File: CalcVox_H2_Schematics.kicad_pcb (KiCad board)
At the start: 4 copper layers, 118.1 x 170.2 mm, 69 parts, among them J1 Battery_Barrel_Jack, J2 AudioJack3_SwitchTR, SW1-25 SW_Push, SW1-26 SW_Push, SW1-27 SW_Push, SW1-28 SW_Push, SW1-29 SW_Push, SW1-30 SW_Push, SW1-31 SW_Push, SW1-32 SW_Push, SW2-25 SW_Push, SW2-26 SW_Push, SW2-27 SW_Push, SW2-28 SW_Push, SW2-29 SW_Push, SW2-30 SW_Push, SW2-31 SW_Push, SW2-32 SW_Push, SW3-25 SW_Push, SW3-26 SW_Push, SW3-27 SW_Push, SW3-28 SW_Push, SW3-29 SW_Push, SW3-30 SW_Push, SW3-31 SW_Push, SW3-32 SW_Push, SW4-25 SW_Push, SW4-26 SW_Push, SW4-27 SW_Push, SW4-28 SW_Push, SW4-29 SW_Push, SW4-30 SW_Push, SW4-31 SW_Push, SW4-32 SW_Push, SW5-25 SW_Push, SW5-26 SW_Push, SW5-27 SW_Push, SW5-28 SW_Push, SW5-29 SW_Push, SW5-30 SW_Push, SW5-31 SW_Push, SW5-32 SW_Push, SW6-25 SW_Push, SW6-26 SW_Push, SW6-27 SW_Push, SW6-28 SW_Push, SW6-29 SW_Push, SW6-30 SW_Push, SW6-31 SW_Push, SW6-32 SW_Push, U1 Teensy4.1, U2 MOUDLE-SEEEDUINO-XIAO-ESP32S3

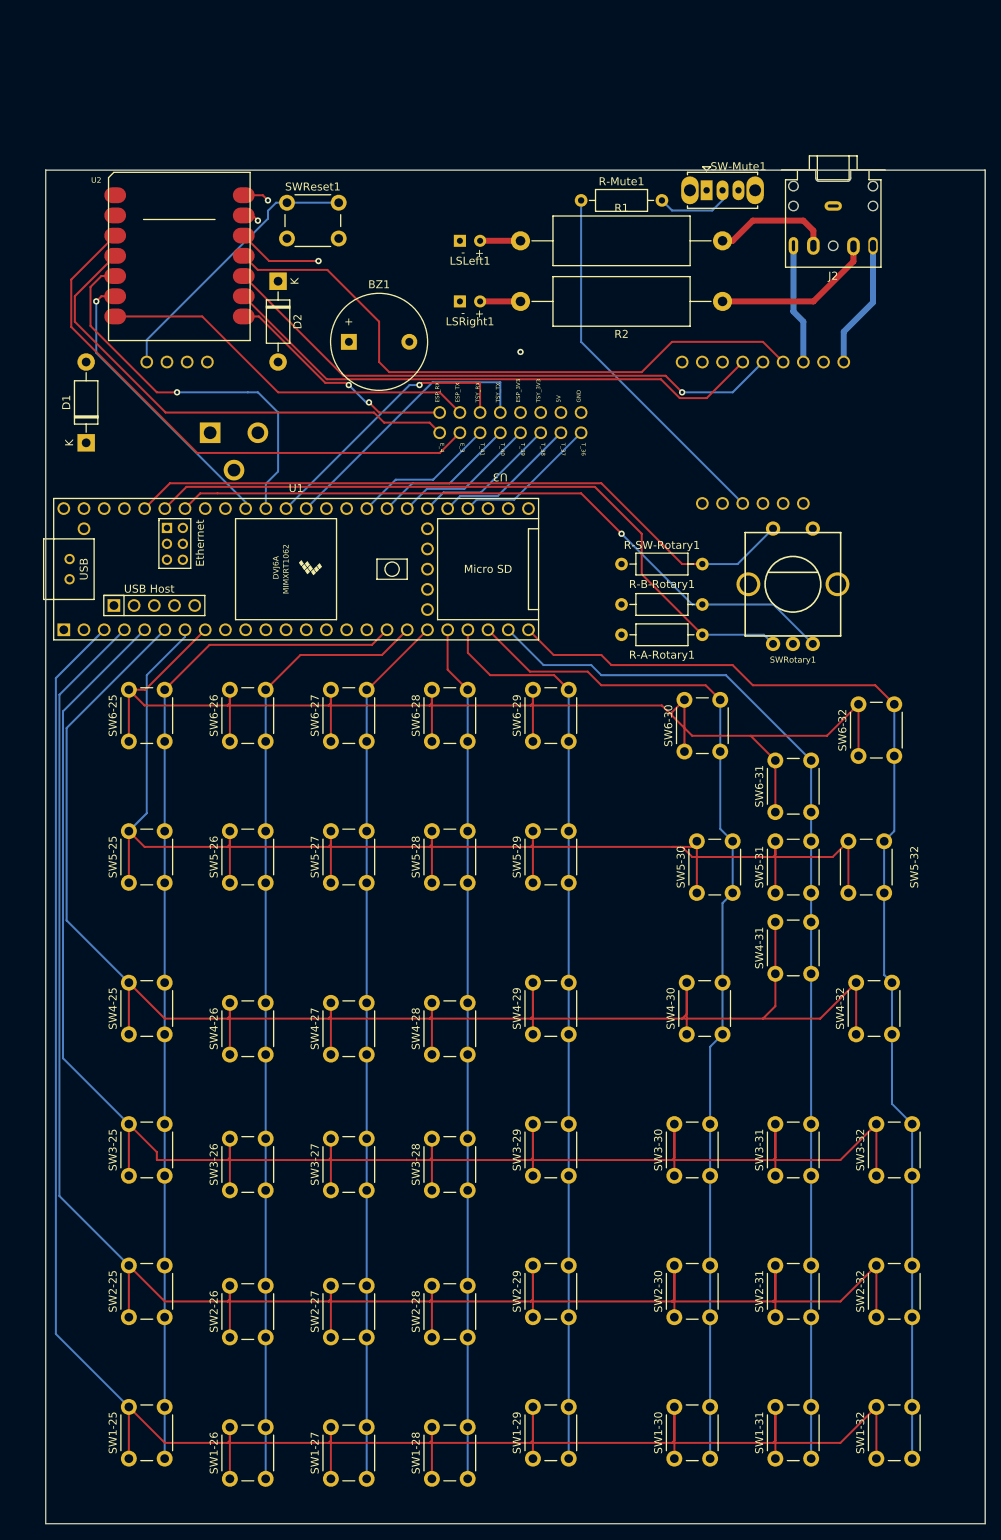
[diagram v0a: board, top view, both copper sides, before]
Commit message: Small change to move board up
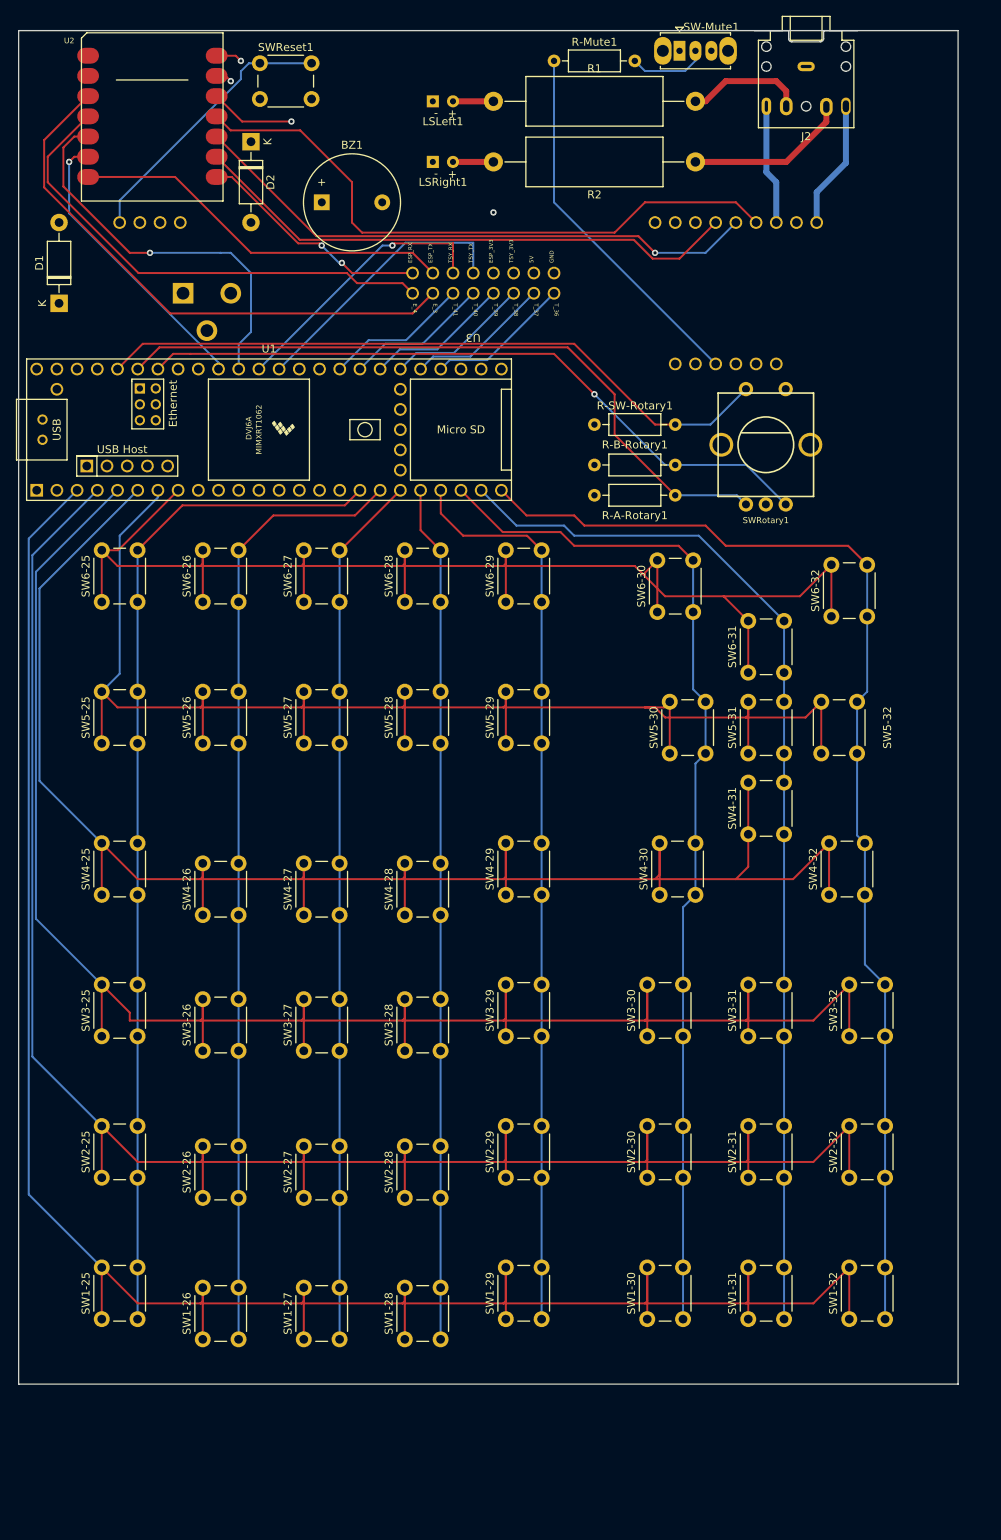
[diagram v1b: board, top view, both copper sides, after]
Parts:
- moved SW2-26 17.9 mm to (71.8, 167.3)
- moved SW2-27 17.9 mm to (84.5, 167.3)
- moved SW2-28 17.9 mm to (97.2, 167.3)
- moved SW4-26 17.9 mm to (71.8, 131.8)
- moved SW4-27 17.9 mm to (84.5, 131.8)
- moved SW4-28 17.9 mm to (97.2, 131.8)
- moved SW6-25 17.9 mm to (59.1, 92.4)
- moved SW6-26 17.9 mm to (71.8, 92.4)
- moved SW6-27 17.9 mm to (84.5, 92.4)
- moved SW6-28 17.9 mm to (97.2, 92.4)
- moved SW6-29 17.9 mm to (109.9, 92.4)
- moved SW6-32 17.9 mm to (150.8, 94.2)
- moved U1 17.9 mm to (80.1, 70.7)
- moved D1 17.9 mm to (53.7, 54.9)
- moved D2 17.9 mm to (77.9, 34.5)
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
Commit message: added readme
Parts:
- added AGND-GND1: SolderJumper_2_Open, Jumper:SolderJumper-2_P1.3mm_Open_TrianglePad1.0x1.5mm, F.Cu at (156.8, 26.7)
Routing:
- net GND: track 2.05 -> 3.32 mm, vias 1 -> 2
- net Net-(A1-AGND): track 0.00 -> 1.09 mm, vias 0 -> 1
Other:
- board text added: "CalcVox H2"
- board text added: "JLCJLCJLCJLC"

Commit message: updated readme
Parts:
- added REF**: MountingHole_2.2mm_M2, MountingHole:MountingHole_2.2mm_M2, F.Cu at (163.8, 24.1)
- added REF**: MountingHole_2.2mm_M2, MountingHole:MountingHole_2.2mm_M2, F.Cu at (52.1, 186.7)
- added REF**: MountingHole_2.2mm_M2, MountingHole:MountingHole_2.2mm_M2, F.Cu at (163.8, 188.0)
- added REF**: MountingHole_2.2mm_M2, MountingHole:MountingHole_2.2mm_M2, F.Cu at (52.1, 24.1)

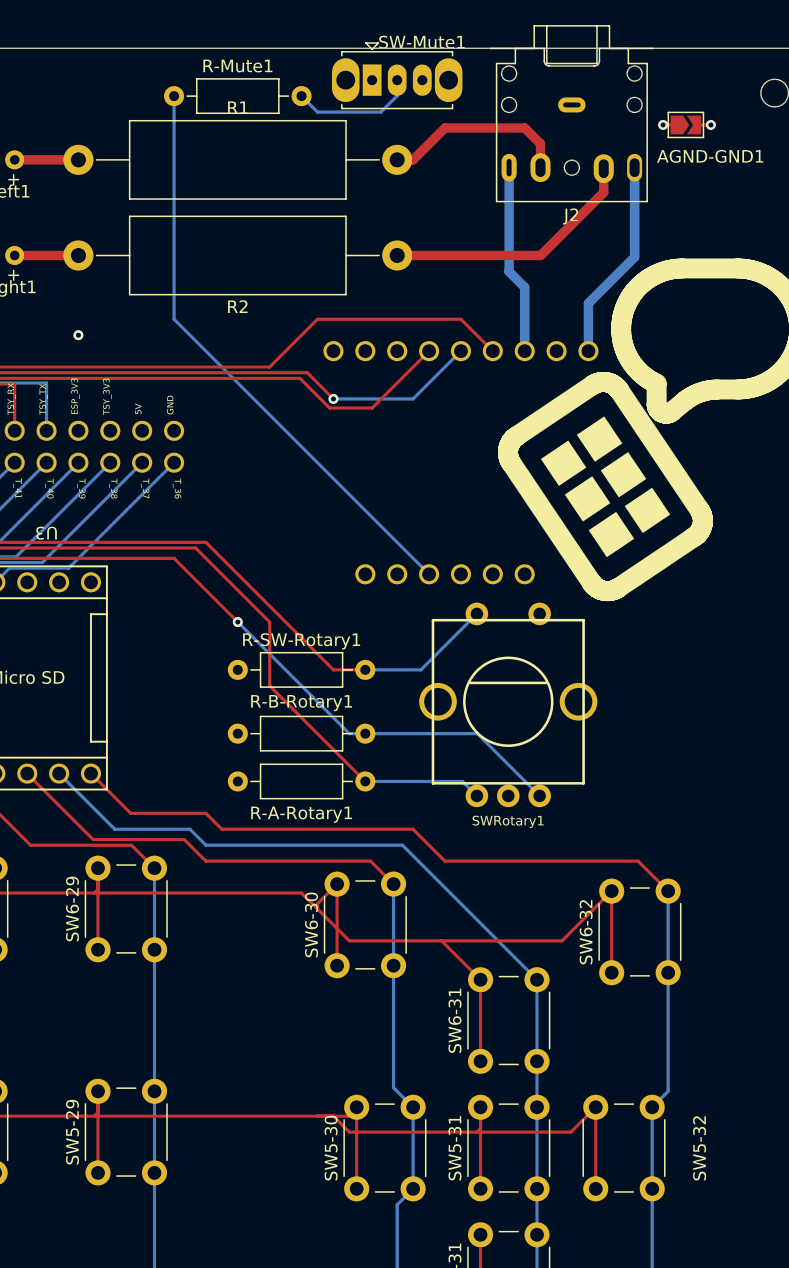
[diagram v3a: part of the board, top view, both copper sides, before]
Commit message: Added 3d models and fixed small mistakes
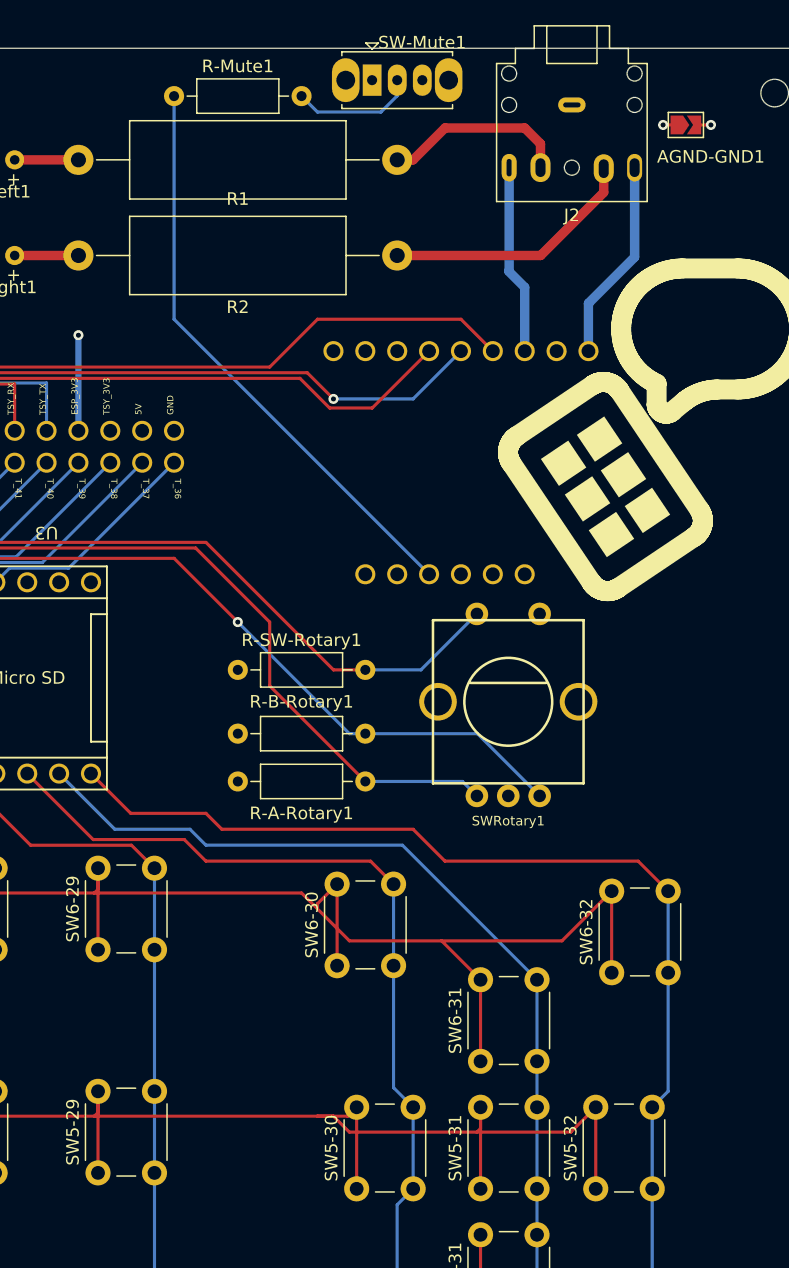
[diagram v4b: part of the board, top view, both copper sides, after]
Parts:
- SW1-25, SW1-26, SW1-27, SW1-28, SW1-29, SW1-30, SW1-31, SW1-32, SW2-25, SW2-26, SW2-27, SW2-28, SW2-29, SW2-30, SW2-31, SW2-32, SW3-25, SW3-26, SW3-27, SW3-28, SW3-29, SW3-30, SW3-31, SW3-32, SW4-25, SW4-26, SW4-27, SW4-28, SW4-29, SW4-30, SW4-31, SW4-32, SW5-25, SW5-26, SW5-27, SW5-28, SW5-29, SW5-30, SW5-31, SW5-32, SW6-25, SW6-26, SW6-27, SW6-28, SW6-29, SW6-30, SW6-31, SW6-32, SWReset1: footprint Button_Switch_THT:SW_PUSH_6mm_H7.3mm_1 -> Button_Switch_THT:SW_PUSH_6mm_H9.5mm
